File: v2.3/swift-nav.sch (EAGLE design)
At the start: 155 parts, among them J1 SMA_EDGE, J6 ZX62-B-5PA, Q1 IRLML6401, U1 6SLX9FTG256, U10 MAX2769, U12 PT7M8206B33TA5EX, U13 M25PX80, U2 LTC3407A_DFN, U3 STM32-M-64-LQFP, U4 7Q-16.368MBG-T, U5 SMA_PATCH_SMDGND, U6 93LC56BT-I/OT, U7 FT232HQ, U8 B4050, U9 XC2401, X3 FPGA DEBUG, X4 NX5032GA-12M, X5 CONN_5-2

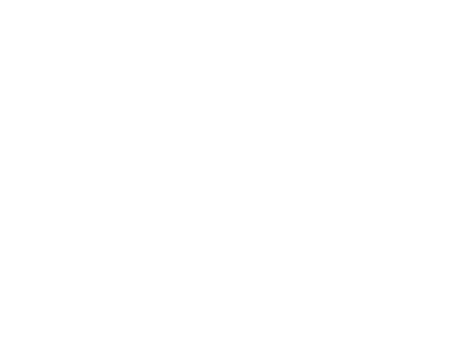
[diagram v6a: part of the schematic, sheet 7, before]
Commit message: Silkscreen and logo updated for v2.3
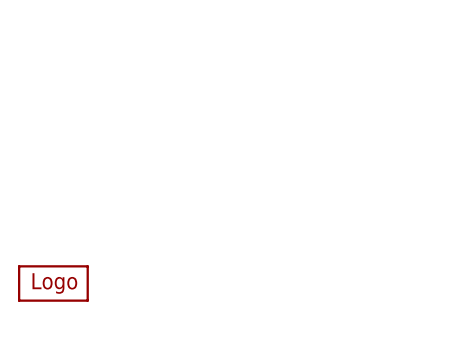
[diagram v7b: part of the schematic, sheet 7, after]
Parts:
- added U$2: LOGOLOGO3_SMALL, swift-nav:LOGOLOGO3_SMALL
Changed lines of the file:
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@@
 <?xml version="1.0" encoding="utf-8"?>
 <!DOCTYPE eagle SYSTEM "eagle.dtd">
-<eagle version="6.2">
+<eagle version="6.1">
 <drawing>
 <settings>
@@
 <part name="C80" library="pel_dipol_comp" deviceset="CAPACITOR" device="-0402" value="0.47uF"/>
 <part name="C81" library="pel_dipol_comp" deviceset="CAPACITOR" device="-0402" value="0.47uF"/>
+<part name="U$2" library="swift-nav" deviceset="LOGO" device="LOGO3_SMALL"/>
 </parts>
 <sheets>
@@
 <attribute name="VALUE" x="113.03" y="187.96" size="1.778" layer="96"/>
 </instance>
+<instance part="U$2" gate="G$1" x="10.16" y="7.62"/>
 </instances>
 <busses>

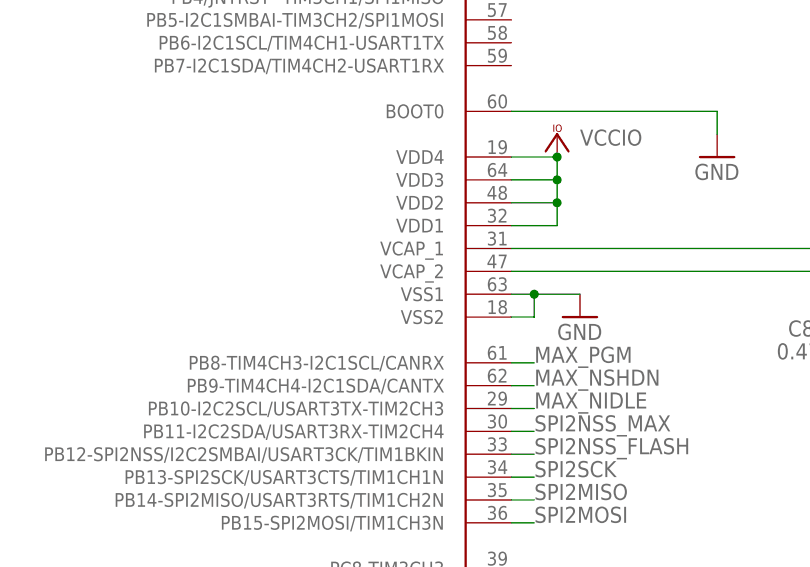
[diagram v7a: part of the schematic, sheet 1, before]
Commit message: Updated footprints and board with proper paste sizes
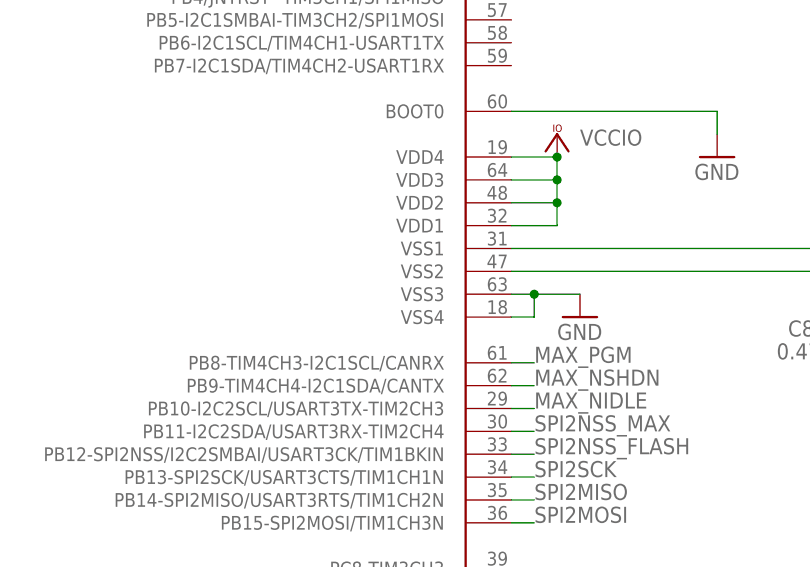
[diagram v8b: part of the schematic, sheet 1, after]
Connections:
- net GND: now also U3.VSS3, U3.VSS4; no longer U3.VSS1, U3.VSS2
- net VSS1: now also U3.VSS1; no longer U3.VCAP_1
- net VSS2: now also U3.VSS2; no longer U3.VCAP_2
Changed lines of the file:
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@@
 <?xml version="1.0" encoding="utf-8"?>
 <!DOCTYPE eagle SYSTEM "eagle.dtd">
-<eagle version="6.1">
+<eagle version="6.2">
 <drawing>
 <settings>
@@
 <wire x1="274.32" y1="132.08" x2="276.86" y2="132.08" width="0.1524" layer="91"/>
 <pinref part="GND53" gate="1" pin="GND"/>
-<pinref part="U3" gate="G$1" pin="VSS1"/>
-<pinref part="U3" gate="G$1" pin="VSS2"/>
+<pinref part="U3" gate="G$1" pin="VSS3"/>
+<pinref part="U3" gate="G$1" pin="VSS4"/>
 <wire x1="276.86" y1="132.08" x2="281.94" y2="132.08" width="0.1524" layer="91"/>
 <wire x1="274.32" y1="129.54" x2="276.86" y2="129.54" width="0.1524" layer="91"/>
@@
 <wire x1="274.32" y1="134.62" x2="312.42" y2="134.62" width="0.1524" layer="91"/>
 <wire x1="312.42" y1="134.62" x2="312.42" y2="132.08" width="0.1524" layer="91"/>
-<pinref part="U3" gate="G$1" pin="VCAP_2"/>
+<pinref part="U3" gate="G$1" pin="VSS2"/>
 <pinref part="C82" gate="G$1" pin="2"/>
 </segment>
@@
 <net name="VSS1" class="0">
 <segment>
-<pinref part="U3" gate="G$1" pin="VCAP_1"/>
+<pinref part="U3" gate="G$1" pin="VSS1"/>
 <wire x1="274.32" y1="137.16" x2="320.04" y2="137.16" width="0.1524" layer="91"/>
 <pinref part="C66" gate="G$1" pin="1"/>
